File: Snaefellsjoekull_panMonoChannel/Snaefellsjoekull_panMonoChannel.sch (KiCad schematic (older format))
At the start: 9 parts, among them J1 AudioJack2_SwitchT, J2 Bus Connector

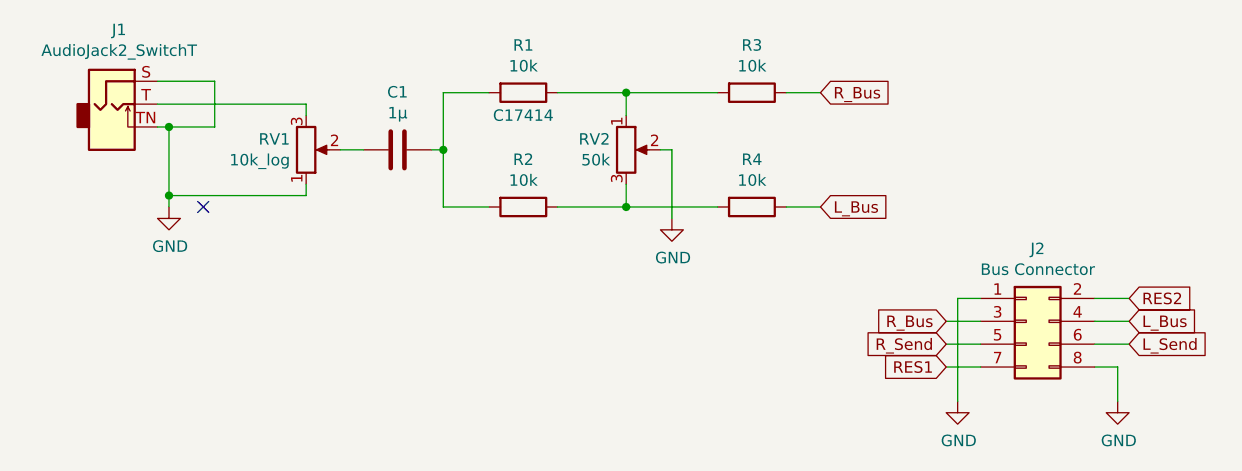
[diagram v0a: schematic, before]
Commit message: Potentiometer fixed
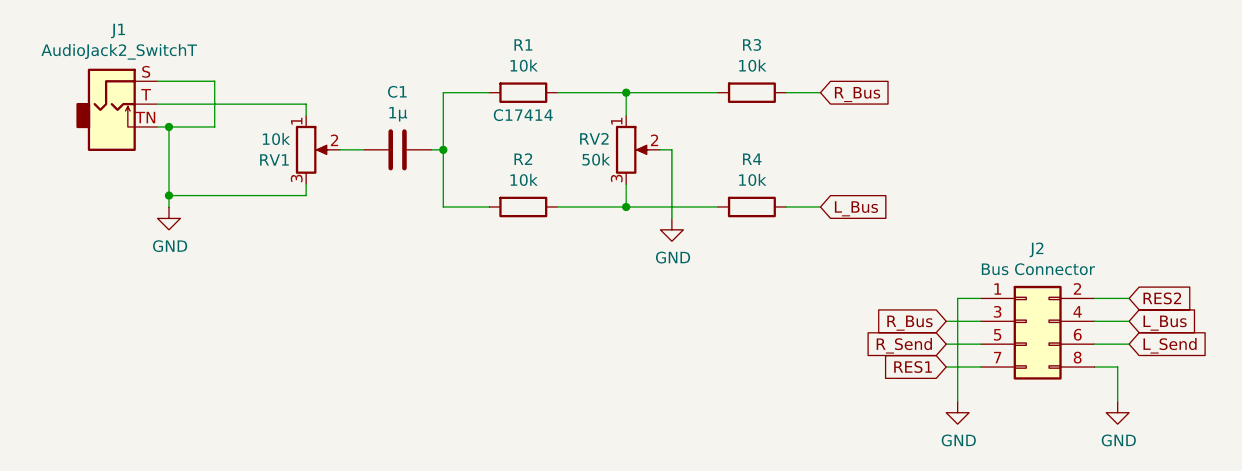
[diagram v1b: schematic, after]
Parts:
- RV1: value 10k_log -> 10k
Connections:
- net GND: now also RV1.3; no longer RV1.1
- net at J1.T: now also RV1.1; no longer RV1.3
- no-connect marks 1 -> 0
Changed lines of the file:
@@
 P 5050 3350
 F 0 "RV1" H 4980 3304 50  0000 R CNN
-F 1 "10k_log" H 4980 3395 50  0000 R CNN
+F 1 "10k" H 4980 3395 50  0000 R CNN
 F 2 "Potentiometer_THT:Potentiometer_Bourns_PTV09A-1_Single_Vertical" H 5050 3350 50  0001 C CNN
 F 3 "~" H 5050 3350 50  0001 C CNN
 	1    5050 3350
-	1    0    0    1
+	1    0    0    -1
 $EndComp
 Wire Wire Line
@@
 Wire Wire Line
 	8600 4300 8600 4450
-NoConn ~ 4600 3600
 $Comp
 L Device:C C1
